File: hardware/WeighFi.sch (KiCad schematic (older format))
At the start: 19 parts, among them J1 USB, P1 CONN_1, P2 CONN_1, P3 CONN_1, U1 MAX1555, U2 MCP1700

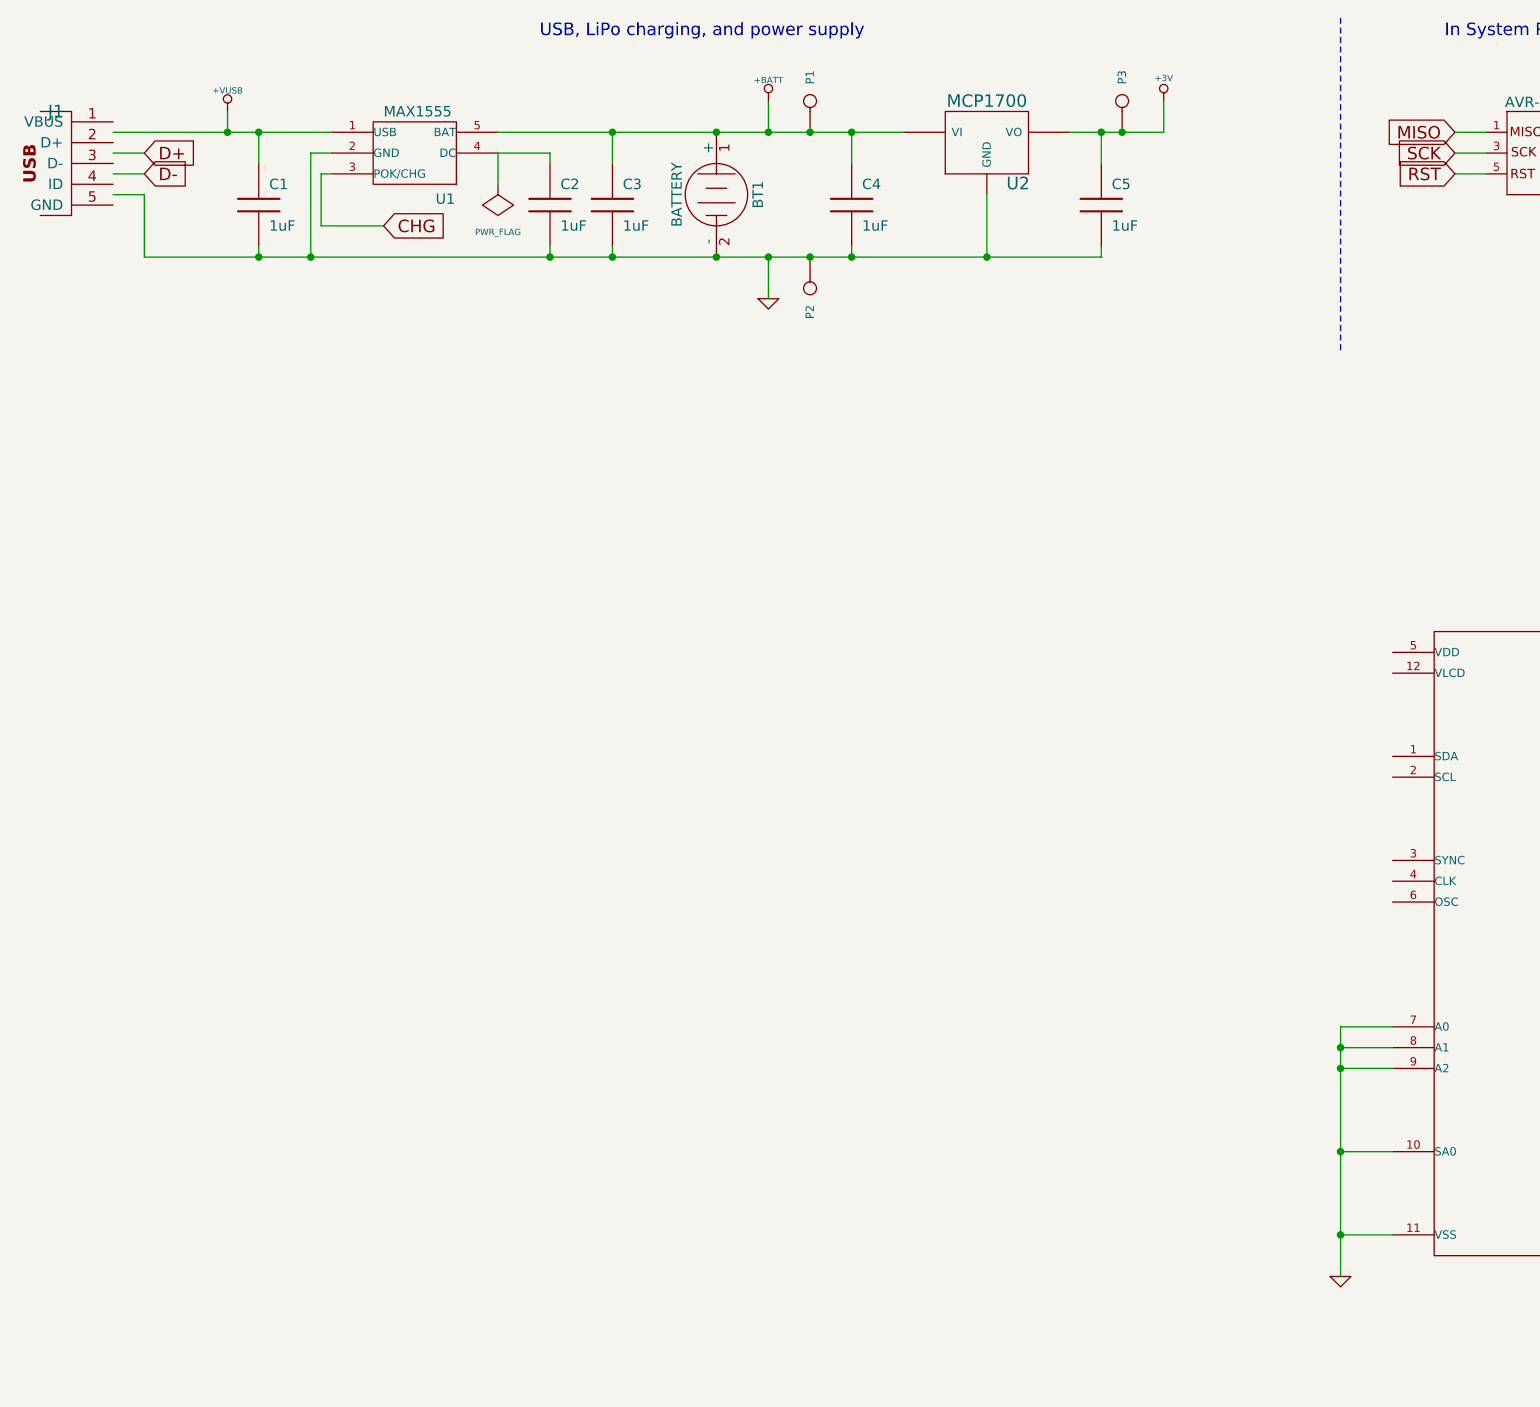
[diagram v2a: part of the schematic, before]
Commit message: Add ADC to schematic
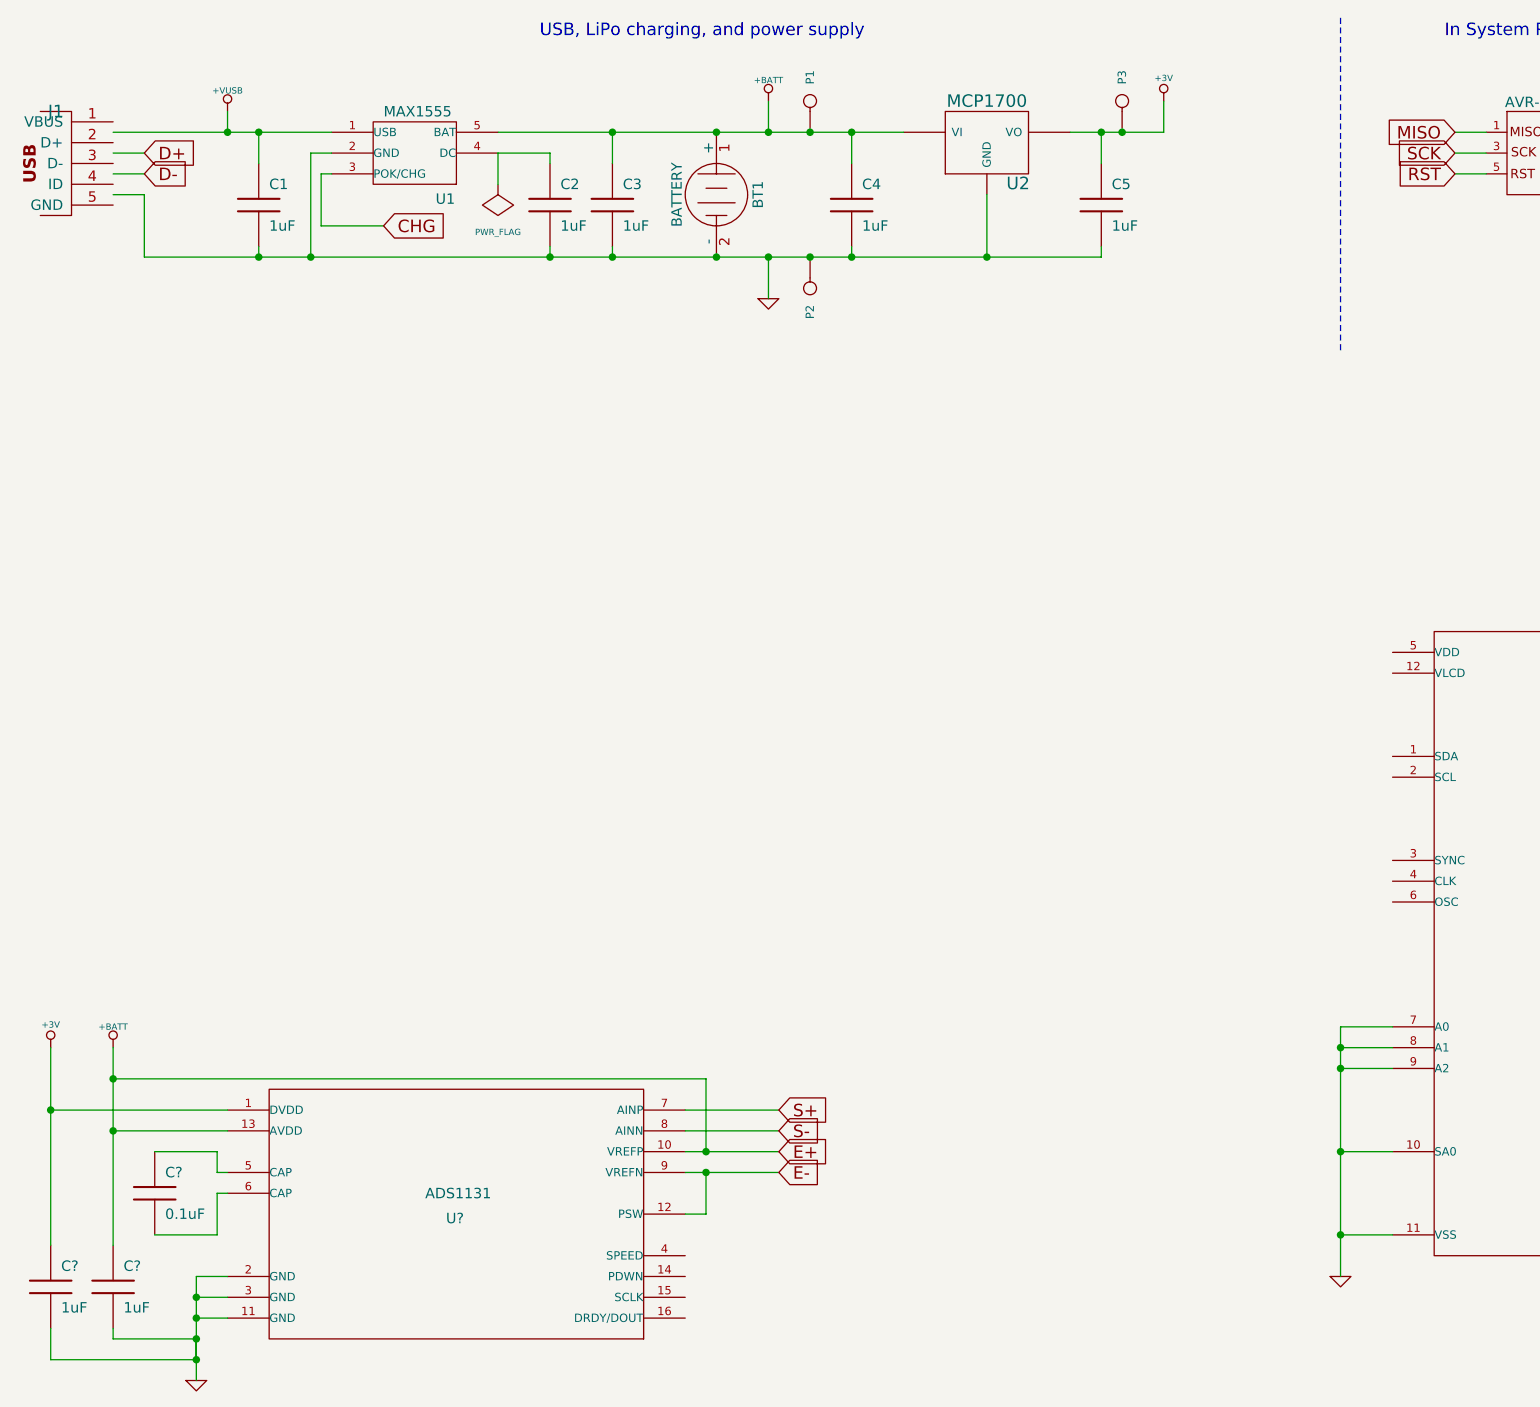
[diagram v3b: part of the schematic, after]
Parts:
- added C? (x2): 1uF, symbol C
- added C?: 0.1uF, symbol C
- added U?: ADS1131, symbol ADS1131
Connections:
- net labels added: E+, E-, S+, S-
- wire segments 75 -> 134
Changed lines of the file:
@@
-EESchema Schematic File Version 2  date Thu 10 May 2012 13:00:41 BST
+EESchema Schematic File Version 2  date Mon 14 May 2012 07:56:18 BST
 LIBS:dresco
 LIBS:power
@@
 Sheet 1 1
 Title "WeighFi"
-Date "10 may 2012"
+Date "14 may 2012"
 Rev "1.0"
 Comp ""
@@
 Comment4 ""
 $EndDescr
+Wire Wire Line
+	900  5550 900  5850
+Wire Wire Line
+	900  5850 900  6500
+Wire Wire Line
+	1400 6050 1700 6050
+Wire Wire Line
+	1700 6050 1700 6150
+Wire Wire Line
+	1700 6150 1750 6150
+Connection ~ 1600 6950
+Wire Wire Line
+	1600 6950 1200 6950
+Wire Wire Line
+	1200 6950 1200 6900
+Connection ~ 900  5850
+Connection ~ 4050 6050
+Connection ~ 1200 5700
+Wire Wire Line
+	1200 5700 4050 5700
+Wire Wire Line
+	4050 5700 4050 6050
+Wire Wire Line
+	3950 6050 4050 6050
+Wire Wire Line
+	4050 6050 4400 6050
+Wire Wire Line
+	4400 5850 3950 5850
+Wire Wire Line
+	1200 5550 1200 5700
+Wire Wire Line
+	1200 5700 1200 5950
+Wire Wire Line
+	1200 5950 1200 6500
+Wire Wire Line
+	1200 5950 1750 5950
+Connection ~ 1600 6750
+Wire Wire Line
+	1750 6750 1600 6750
 Connection ~ 7100 6450
 Wire Wire Line
@@
 Connection ~ 7100 5650
 Wire Wire Line
-	7350 5650 7100 5650
-Wire Wire Line
-	7100 6650 7100 5450
+	7100 5650 7350 5650
+Wire Wire Line
+	7100 6650 7100 6450
+Wire Wire Line
+	7100 6450 7100 6050
+Wire Wire Line
+	7100 6050 7100 5650
+Wire Wire Line
+	7100 5650 7100 5550
+Wire Wire Line
+	7100 5550 7100 5450
 Wire Wire Line
 	7100 5450 7350 5450
@@
 Connection ~ 4100 1150
 Wire Wire Line
-	5000 1150 3050 1150
+	5000 1150 4750 1150
+Wire Wire Line
+	4750 1150 4550 1150
+Wire Wire Line
+	4550 1150 4350 1150
+Wire Wire Line
+	4350 1150 4100 1150
+Wire Wire Line
+	4100 1150 3600 1150
+Wire Wire Line
+	3600 1150 3050 1150
 Wire Notes Line
 	7100 600  7100 2200
@@
 Connection ~ 3600 1150
 Wire Wire Line
-	3600 1150 3600 1300
+	3600 1300 3600 1150
 Wire Wire Line
 	1900 1300 1900 1150
@@
 	5950 1700 5950 1750
 Wire Wire Line
-	6250 1150 5800 1150
+	6250 1150 6050 1150
+Wire Wire Line
+	6050 1150 5950 1150
+Wire Wire Line
+	5950 1150 5800 1150
 Wire Wire Line
 	7800 1250 7650 1250
@@
 	8550 1150 8550 900
 Wire Wire Line
-	4750 1300 4750 1150
+	4750 1150 4750 1300
 Connection ~ 2150 1750
 Wire Wire Line
@@
 	1200 1250 1350 1250
 Wire Wire Line
-	2250 1150 1200 1150
+	2250 1150 1900 1150
+Wire Wire Line
+	1900 1150 1750 1150
+Wire Wire Line
+	1750 1150 1200 1150
 Connection ~ 1750 1150
 Wire Notes Line
 	9100 600  9100 2200
 Wire Wire Line
-	5950 1750 1350 1750
+	5950 1750 5400 1750
+Wire Wire Line
+	5400 1750 4750 1750
+Wire Wire Line
+	4750 1750 4550 1750
+Wire Wire Line
+	4550 1750 4350 1750
+Wire Wire Line
+	4350 1750 4100 1750
+Wire Wire Line
+	4100 1750 3600 1750
+Wire Wire Line
+	3600 1750 3300 1750
+Wire Wire Line
+	3300 1750 2150 1750
+Wire Wire Line
+	2150 1750 1900 1750
+Wire Wire Line
+	1900 1750 1350 1750
 Connection ~ 3600 1750
 Connection ~ 4100 1750
@@
 Connection ~ 7100 5550
 Wire Wire Line
-	7350 6050 7100 6050
+	7100 6050 7350 6050
 Connection ~ 7100 6050
+Wire Wire Line
+	1750 6650 1600 6650
+Wire Wire Line
+	1600 6650 1600 6750
+Wire Wire Line
+	1600 6750 1600 6850
+Wire Wire Line
+	1600 6850 1600 6950
+Wire Wire Line
+	1600 6950 1600 7050
+Wire Wire Line
+	1600 7050 1600 6950
+Wire Wire Line
+	1600 6950 1600 7050
+Wire Wire Line
+	1600 7050 1600 7150
+Wire Wire Line
+	1600 6850 1750 6850
+Connection ~ 1600 6850
+Wire Wire Line
+	900  5850 1750 5850
+Wire Wire Line
+	4400 5950 3950 5950
+Wire Wire Line
+	3950 6150 4050 6150
+Wire Wire Line
+	4050 6150 4400 6150
+Wire Wire Line
+	4050 6150 4050 6350
+Wire Wire Line
+	4050 6350 3950 6350
+Connection ~ 4050 6150
+Connection ~ 1200 5950
+Wire Wire Line
+	900  6900 900  7050
+Wire Wire Line
+	900  7050 1600 7050
+Connection ~ 1600 7050
+Wire Wire Line
+	1750 6250 1700 6250
+Wire Wire Line
+	1700 6250 1700 6450
+Wire Wire Line
+	1700 6450 1400 6450
+$Comp
+L +3V #PWR?
+U 1 1 4FB0AACD
+P 900 5550
+F 0 "#PWR?" H 900 5460 30  0001 C CNN
+F 1 "+3V" H 900 5660 30  0000 C CNN
+	1    900  5550
+	1    0    0    -1
+$EndComp
+$Comp
+L C C?
+U 1 1 4FB0A71F
+P 1400 6250
+F 0 "C?" H 1450 6350 50  0000 L CNN
+F 1 "0.1uF" H 1450 6150 50  0000 L CNN
+	1    1400 6250
+	1    0    0    -1
+$EndComp
+$Comp
+L C C?
+U 1 1 4FB0A71B
+P 1200 6700
+F 0 "C?" H 1250 6800 50  0000 L CNN
+F 1 "1uF" H 1250 6600 50  0000 L CNN
+	1    1200 6700
+	1    0    0    -1
+$EndComp
+$Comp
+L ADS1131 U?
+U 1 1 4FB0A641
+P 2850 6350
+F 0 "U?" H 2800 6300 50  0000 L BNN
+F 1 "ADS1131" H 2700 6420 50  0000 L BNN
+	1    2850 6350
+	1    0    0    -1
+$EndComp
+$Comp
+L C C?
+U 1 1 4FB0A5B8
+P 900 6700
+F 0 "C?" H 950 6800 50  0000 L CNN
+F 1 "1uF" H 950 6600 50  0000 L CNN
+	1    900  6700
+	1    0    0    -1
+$EndComp
+$Comp
+L +BATT #PWR?
+U 1 1 4FB0A598
+P 1200 5550
+F 0 "#PWR?" H 1200 5500 20  0001 C CNN
+F 1 "+BATT" H 1200 5650 30  0000 C CNN
+	1    1200 5550
+	1    0    0    -1
+$EndComp
 $Comp
 L GND #PWR?
+U 1 1 4FB0A559
+P 1600 7150
+F 0 "#PWR?" H 1600 7150 30  0001 C CNN
+F 1 "GND" H 1600 7080 30  0001 C CNN
+	1    1600 7150
+	1    0    0    -1
+$EndComp
+Text GLabel 4400 5850 2    60   Input ~ 0
+S+
+Text GLabel 4400 5950 2    60   Input ~ 0
+S-
+Text GLabel 4400 6050 2    60   Input ~ 0
+E+
+Text GLabel 4400 6150 2    60   Input ~ 0
+E-
+$Comp
+L GND #PWR?

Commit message: Changed schematic to A3, added RN-171 wireless module  - see how A3 works out, multiple A4 sheets may be better
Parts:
- added MOD?: RN-171, symbol RN-171
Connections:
- wire segments 134 -> 156
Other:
- note added: "ADC"
- moved on the sheet: C?, P?, U?
